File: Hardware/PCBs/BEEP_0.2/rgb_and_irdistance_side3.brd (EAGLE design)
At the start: 12.7 x 17.7 mm, 5 parts, among them IC1 HSDL-9100

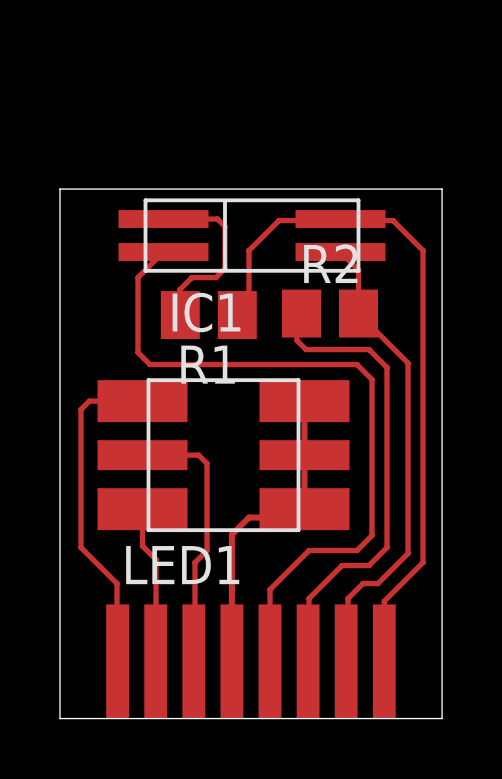
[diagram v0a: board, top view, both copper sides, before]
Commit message: add more distance boards continue work on bottom pcb
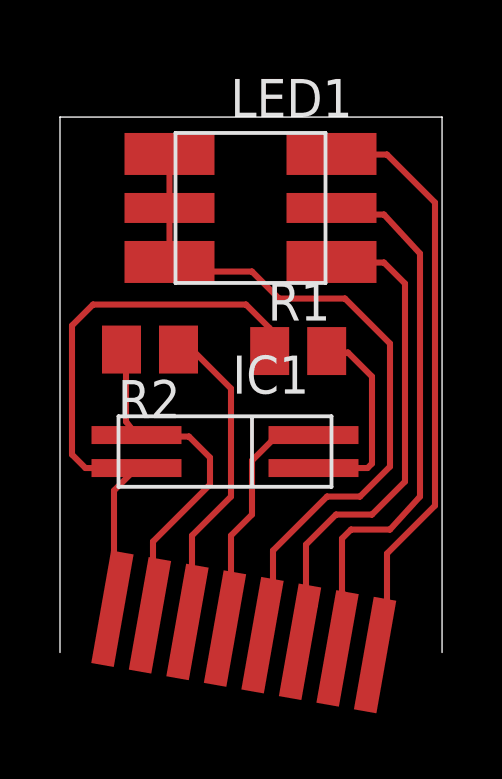
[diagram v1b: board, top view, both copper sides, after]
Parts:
- moved LED1 8.29 mm to (6.35, 17.2), turned to 180 degrees
- moved IC1 7.26 mm to (5.50, 9.10), turned to 180 degrees
- moved R2 6.12 mm to (3.00, 12.5), turned to 180 degrees
- moved R1 3.21 mm to (7.94, 12.4), turned to 0 degrees
- moved U$1 1.86 mm to (5.50, 3.20), turned to 350 degrees
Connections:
- net RGB_ANODE_1: now also U$1.P$8; no longer U$1.P$7
- net RGB_ANODE_2: now also U$1.P$7; no longer U$1.P$6
- net RGB_ANODE_3: now also U$1.P$6; no longer U$1.P$8
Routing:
- net RGB_ANODE_1: track 5.27 -> 20.0 mm
- net IR_LED_K: track 23.6 -> 9.62 mm
- net RGB_COMMON_K: track 11.6 -> 24.1 mm
- net RGB_ANODE_2: track 9.03 -> 18.8 mm
- net RGB_ANODE_3: track 11.1 -> 17.0 mm
- net GND: track 15.7 -> 11.0 mm
- net ADISTANCE: track 15.7 -> 11.9 mm
- net +5V: track 23.2 -> 19.6 mm
- net N$2: track 6.20 -> 6.77 mm
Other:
- board size 12.7 x 17.7 mm -> 12.7 x 17.9 mm
